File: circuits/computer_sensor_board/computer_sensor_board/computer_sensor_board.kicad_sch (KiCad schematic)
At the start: 12 parts, among them J2 Conn_Jetson, J5 Conn_VLP16, J6 Conn_Main_DCDC, J7 Conn_Router

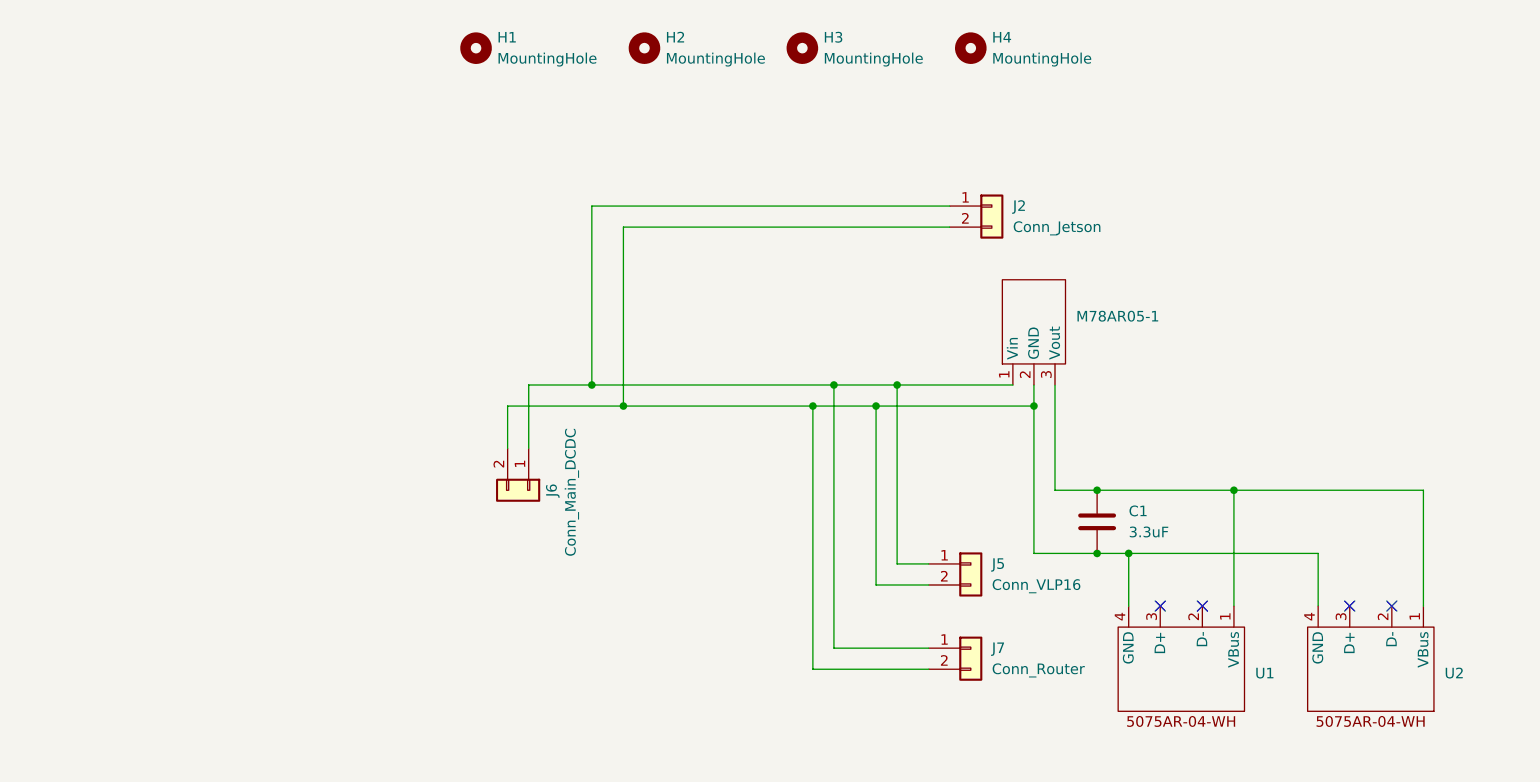
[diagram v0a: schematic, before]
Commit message: fix board design
Signed-off-by: Masaya Kataoka <ms.kataoka@gmail.com>
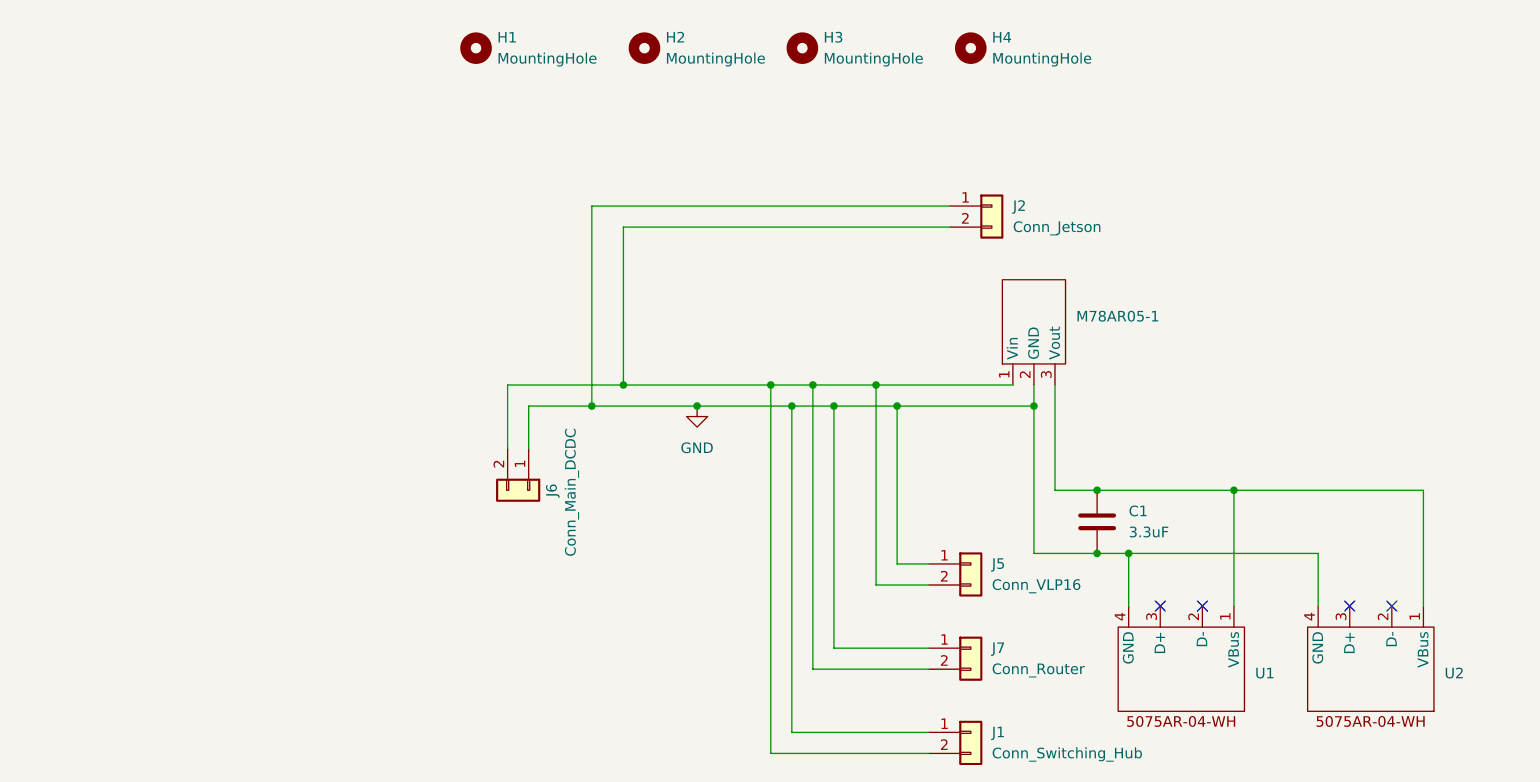
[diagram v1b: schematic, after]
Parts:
- added J1: Conn_Switching_Hub, Connector_AMASS:AMASS_XT30PW-F_1x02_P2.50mm_Horizontal, symbol Connector_Generic:Conn_01x02
- J6: footprint Connector_AMASS:AMASS_XT30PW-F_1x02_P2.50mm_Horizontal -> AMASS_XT60PW-F_1x02_P7.20mm_Horizontal
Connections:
- net at J2.2 (Pin_2), J5.2 (Pin_2), J6.2 (Pin_2)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: now also M78AR05-1.1 (Vin), J1.2 (Pin_2); no longer C1.2, M78AR05-1.2 (GND), U1.4 (GND), U2.4 (GND)
- net GND: now reaches J2.1 (Pin_1), J5.1 (Pin_1), J6.1 (Pin_1), J7.1 (Pin_1)
- net GND: now also C1.2, M78AR05-1.2 (GND), U1.4 (GND), U2.4 (GND), J1.1 (Pin_1); no longer M78AR05-1.1 (Vin)

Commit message: Fix/care invert connection (#378)
* add smart battery board

Signed-off-by: Masaya Kataoka <ms.kataoka@gmail.com>

* fix board design

Signed-off-by: Masaya Kataoka <ms.kataoka@gmail.com>

* change Pch MOSFET

Signed-off-by: Masaya Kataoka <ms.kataoka@gmail.com>

* add heatsink

Signed-off-by: Masaya Kataoka <ms.kataoka@gmail.com>

* remove warning

Signed-off-by: Masaya Kataoka <ms.kataoka@gmail.com>

---------

Signed-off-by: Masaya Kataoka <ms.kataoka@gmail.com>
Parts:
- added D1: LED, LED_THT:LED_D3.0mm, symbol Device:LED
- added HS1: Heatsink, 16PB017-01025:16PB017-01025, symbol Mechanical:Heatsink
- added Q2: 2SJ555-E, Package_TO_SOT_THT:TO-3P-3_Vertical, symbol Device:Q_PMOS_GDS
- added R1: 100K, R_Axial_DIN0207_L6.3mm_D2.5mm_P10.16mm_Horizontal, symbol Device:R
- added R2: 390, R_Axial_DIN0207_L6.3mm_D2.5mm_P10.16mm_Horizontal, symbol Device:R
- added U3: Heatsink_sheet, 16PB017-01025:TO-3PH, symbol TO-3PH:TO-3PH
- J2: footprint Connector_AMASS:AMASS_XT30PW-F_1x02_P2.50mm_Horizontal -> AMASS_XT60PW-F_1x02_P7.20mm_Horizontal
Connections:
- net GND: now also Q2.1 (G), R1.2, R2.2
- net at J1.2 (Pin_2), J2.2 (Pin_2), J5.2 (Pin_2)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: now also D1.2 (A), Q2.3 (S); no longer J6.2 (Pin_2)
- new net: J6.2 (Pin_2), Q2.2 (D), R1.1
- new net: D1.1 (K), R2.1
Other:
- moved on the sheet: J6
